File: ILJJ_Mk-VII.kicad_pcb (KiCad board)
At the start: 2 copper layers, 48.3 x 99.1 mm, 25 parts, among them J1 Conn_02x12, U1 74LS00, U10 74LS00, U11 74LS00, U2 74LS00, U3 74LS00, U4 74LS00, U5 74LS00, U6 74LS00, U7 74LS00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

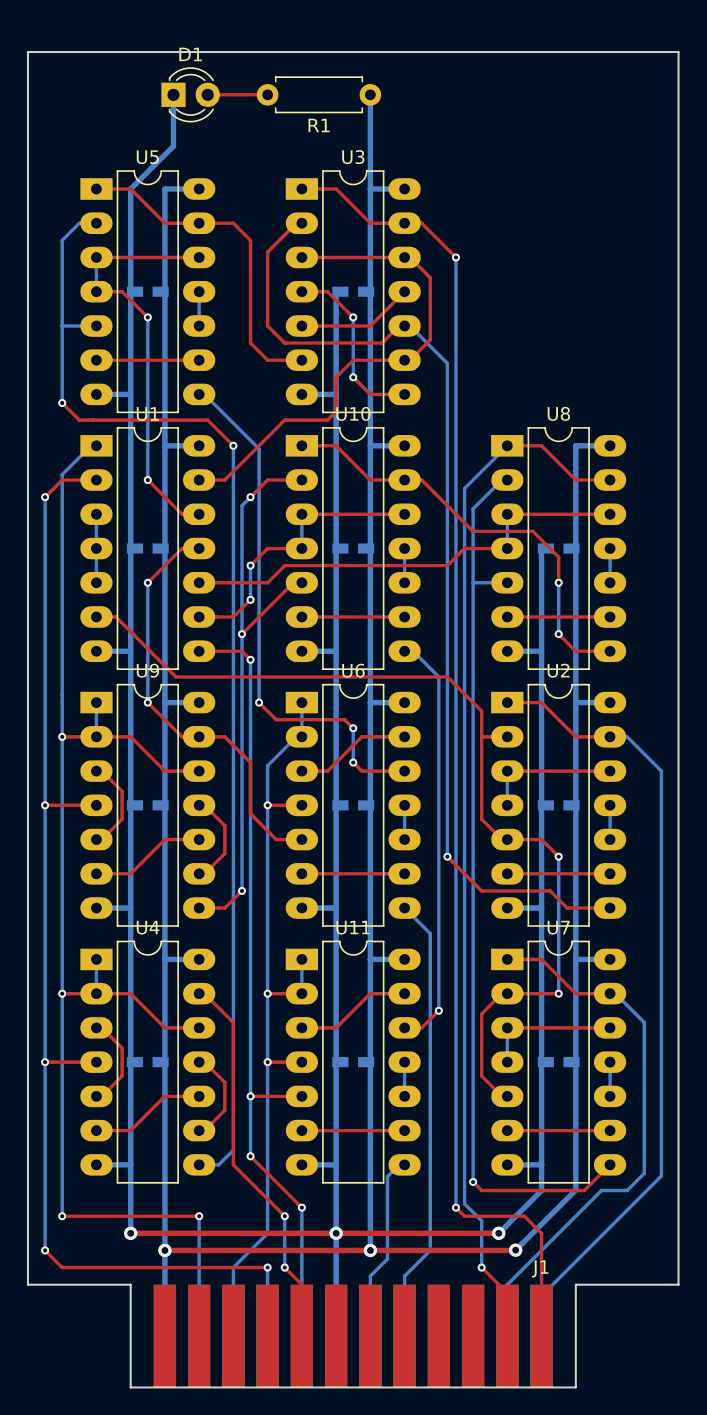
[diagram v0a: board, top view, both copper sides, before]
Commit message: [clean] 配線を微調整
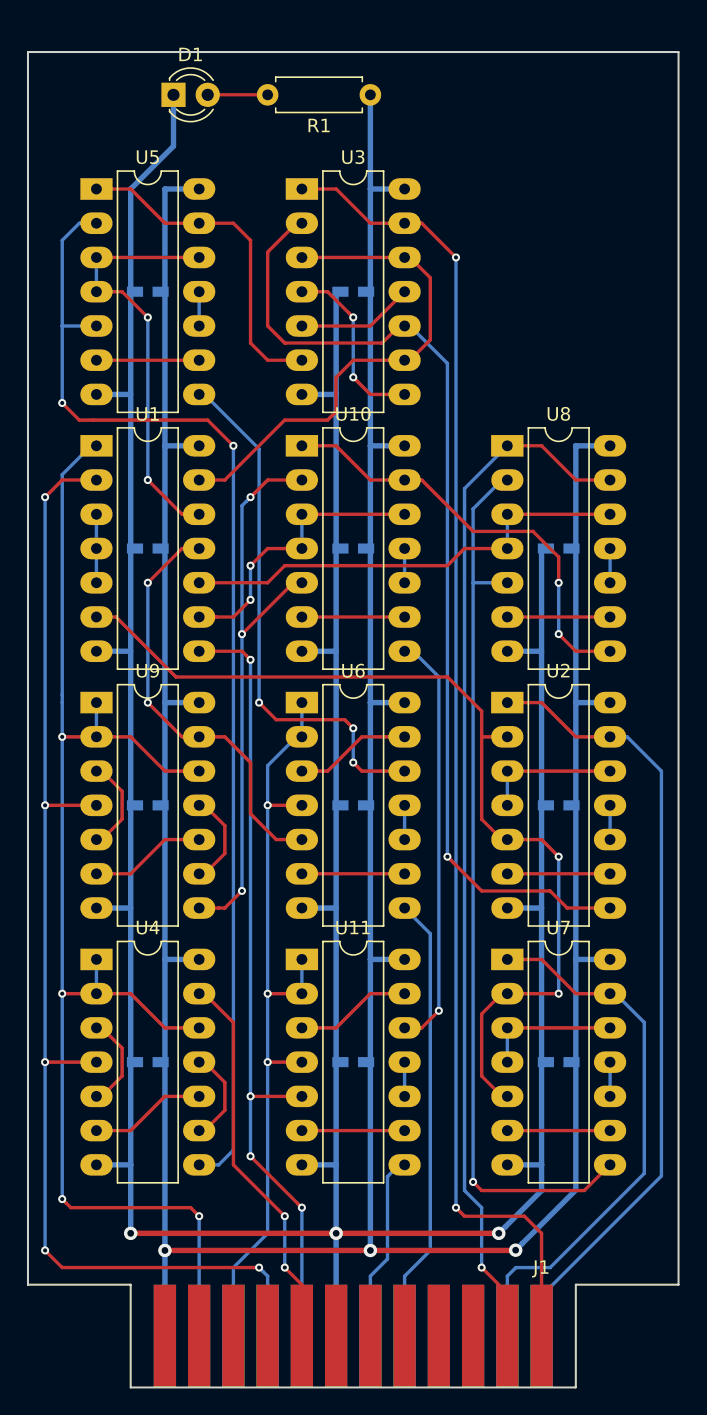
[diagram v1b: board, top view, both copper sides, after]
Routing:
- net /F2: track 105.0 -> 104.2 mm
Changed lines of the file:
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@@
     (thickness 1.6)
     (drawings 8)
-    (tracks 447)
+    (tracks 453)
     (zones 0)
     (modules 25)
@@
   (segment (start 111.76 104.14) (end 109.22 101.6) (width 0.25) (layer F.Cu) (net 4))
   (segment (start 106.68 101.6) (end 106.68 99.06) (width 0.25) (layer B.Cu) (net 4))
-  (via (at 114.3 137.16) (size 0.6) (drill 0.3) (layers F.Cu B.Cu) (net 4))
-  (segment (start 114.3 146.05) (end 114.3 137.16) (width 0.25) (layer B.Cu) (net 4))
-  (via (at 104.14 137.16) (size 0.6) (drill 0.3) (layers F.Cu B.Cu) (net 4))
-  (segment (start 114.3 137.16) (end 104.14 137.16) (width 0.25) (layer F.Cu) (net 4))
   (segment (start 106.28 80.01) (end 104.14 82.15) (width 0.25) (layer B.Cu) (net 4))
   (segment (start 104.14 98.494315) (end 104.14 99.06) (width 0.25) (layer B.Cu) (net 4))
@@
   (segment (start 104.14 101.6) (end 104.14 99.06) (width 0.25) (layer B.Cu) (net 4))
   (segment (start 106.68 101.6) (end 104.14 101.6) (width 0.25) (layer F.Cu) (net 4))
-  (segment (start 104.14 137.16) (end 104.14 101.6) (width 0.25) (layer B.Cu) (net 4))
   (via (at 104.14 120.65) (size 0.6) (drill 0.3) (layers F.Cu B.Cu) (net 4))
   (segment (start 106.68 120.65) (end 104.14 120.65) (width 0.25) (layer F.Cu) (net 4))
+  (via (at 114.3 137.16) (size 0.6) (drill 0.3) (layers F.Cu B.Cu) (net 4))
+  (segment (start 114.3 146.05) (end 114.3 137.16) (width 0.25) (layer B.Cu) (net 4))
+  (via (at 104.14 135.89) (size 0.6) (drill 0.3) (layers F.Cu B.Cu) (net 4))
+  (segment (start 104.14 101.6) (end 104.14 135.89) (width 0.25) (layer B.Cu) (net 4))
+  (segment (start 104.775 136.525) (end 104.439999 136.189999) (width 0.25) (layer F.Cu) (net 4))
+  (segment (start 104.439999 136.189999) (end 104.14 135.89) (width 0.25) (layer F.Cu) (net 4))
+  (segment (start 113.665 136.525) (end 104.775 136.525) (width 0.25) (layer F.Cu) (net 4))
+  (segment (start 114.3 137.16) (end 113.665 136.525) (width 0.25) (layer F.Cu) (net 4))
   (segment (start 116.84 146.05) (end 116.84 140.97) (width 0.25) (layer B.Cu) (net 5))
   (segment (start 116.84 140.97) (end 119.38 138.43) (width 0.25) (layer B.Cu) (net 5))
@@
   (segment (start 119.38 125.73) (end 119.38 120.65) (width 0.25) (layer B.Cu) (net 5))
   (segment (start 119.38 138.43) (end 119.38 125.73) (width 0.25) (layer B.Cu) (net 5))
-  (via (at 119.38 140.97) (size 0.6) (drill 0.3) (layers F.Cu B.Cu) (net 6))
-  (segment (start 119.38 146.05) (end 119.38 140.97) (width 0.25) (layer B.Cu) (net 6))
   (via (at 102.87 139.7) (size 0.6) (drill 0.3) (layers F.Cu B.Cu) (net 6))
-  (segment (start 104.14 140.97) (end 102.87 139.7) (width 0.25) (layer F.Cu) (net 6))
-  (segment (start 119.38 140.97) (end 104.14 140.97) (width 0.25) (layer F.Cu) (net 6))
   (via (at 102.87 83.82) (size 0.6) (drill 0.3) (layers F.Cu B.Cu) (net 6))
   (segment (start 104.14 82.55) (end 102.87 83.82) (width 0.25) (layer F.Cu) (net 6))
@@
   (segment (start 102.87 125.73) (end 102.87 106.68) (width 0.25) (layer B.Cu) (net 6))
   (segment (start 102.87 139.7) (end 102.87 125.73) (width 0.25) (layer B.Cu) (net 6))
+  (via (at 118.745 140.97) (size 0.6) (drill 0.3) (layers F.Cu B.Cu) (net 6))
+  (segment (start 119.38 141.605) (end 119.044999 141.269999) (width 0.25) (layer B.Cu) (net 6))
+  (segment (start 119.044999 141.269999) (end 118.745 140.97) (width 0.25) (layer B.Cu) (net 6))
+  (segment (start 102.87 139.7) (end 104.14 140.97) (width 0.25) (layer F.Cu) (net 6))
+  (segment (start 104.14 140.97) (end 118.320736 140.97) (width 0.25) (layer F.Cu) (net 6))
+  (segment (start 119.38 146.05) (end 119.38 141.605) (width 0.25) (layer B.Cu) (net 6))
+  (segment (start 118.320736 140.97) (end 118.745 140.97) (width 0.25) (layer F.Cu) (net 6))
   (segment (start 121.92 146.05) (end 121.92 143.0655) (width 0.25) (layer F.Cu) (net 7))
   (segment (start 121.92 142.24) (end 120.65 140.97) (width 0.25) (layer F.Cu) (net 7))
@@
   (segment (start 137.16 142.875) (end 135.255 140.97) (width 0.25) (layer F.Cu) (net 17))
   (segment (start 137.16 143.0655) (end 137.16 142.875) (width 0.25) (layer F.Cu) (net 17))
-  (segment (start 135.255 137.504998) (end 133.985 136.234998) (width 0.25) (layer B.Cu) (net 17))
-  (segment (start 135.255 140.97) (end 135.255 137.504998) (width 0.25) (layer B.Cu) (net 17))
-  (segment (start 133.985 136.234998) (end 133.985 83.185) (width 0.25) (layer B.Cu) (net 17))
   (segment (start 133.985 83.185) (end 137.16 80.01) (width 0.25) (layer B.Cu) (net 17))
+  (segment (start 133.985 135.255) (end 133.985 83.185) (width 0.25) (layer B.Cu) (net 17))
+  (segment (start 135.255 136.525) (end 133.985 135.255) (width 0.25) (layer B.Cu) (net 17))
+  (segment (start 135.255 140.97) (end 135.255 136.525) (width 0.25) (layer B.Cu) (net 17))
   (segment (start 139.7 118.11) (end 142.24 120.65) (width 0.25) (layer F.Cu) (net 18))
   (segment (start 142.24 120.65) (end 144.78 120.65) (width 0.25) (layer F.Cu) (net 18))
   (segment (start 137.16 118.11) (end 139.7 118.11) (width 0.25) (layer F.Cu) (net 18))
+  (segment (start 145.18 120.65) (end 144.78 120.65) (width 0.25) (layer B.Cu) (net 18))
   (segment (start 147.32 122.79) (end 145.18 120.65) (width 0.25) (layer B.Cu) (net 18))
-  (segment (start 146.05 135.255) (end 147.32 133.985) (width 0.25) (layer B.Cu) (net 18))
-  (segment (start 144.145 135.255) (end 146.05 135.255) (width 0.25) (layer B.Cu) (net 18))
-  (segment (start 137.16 146.05) (end 137.16 142.24) (width 0.25) (layer B.Cu) (net 18))
+  (segment (start 137.16 146.05) (end 137.16 141.605) (width 0.25) (layer B.Cu) (net 18))
   (segment (start 147.32 133.985) (end 147.32 122.79) (width 0.25) (layer B.Cu) (net 18))
-  (segment (start 145.18 120.65) (end 144.78 120.65) (width 0.25) (layer B.Cu) (net 18))
-  (segment (start 137.16 142.24) (end 144.145 135.255) (width 0.25) (layer B.Cu) (net 18))
+  (segment (start 137.795 140.97) (end 140.335 140.97) (width 0.25) (layer B.Cu) (net 18))
+  (segment (start 140.335 140.97) (end 147.32 133.985) (width 0.25) (layer B.Cu) (net 18))
+  (segment (start 137.16 141.605) (end 137.795 140.97) (width 0.25) (layer B.Cu) (net 18))
   (segment (start 121.92 60.96) (end 124.46 60.96) (width 0.25) (layer F.Cu) (net 19))
   (segment (start 124.46 60.96) (end 127 63.5) (width 0.25) (layer F.Cu) (net 19))

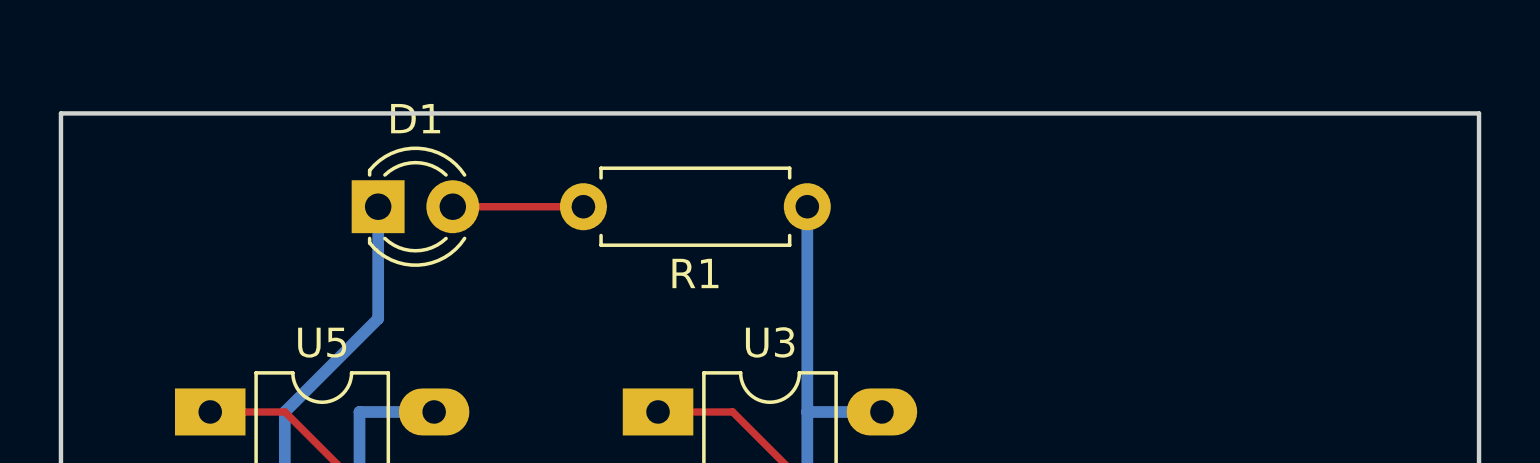
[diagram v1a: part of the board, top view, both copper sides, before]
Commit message: [add] ネジ穴
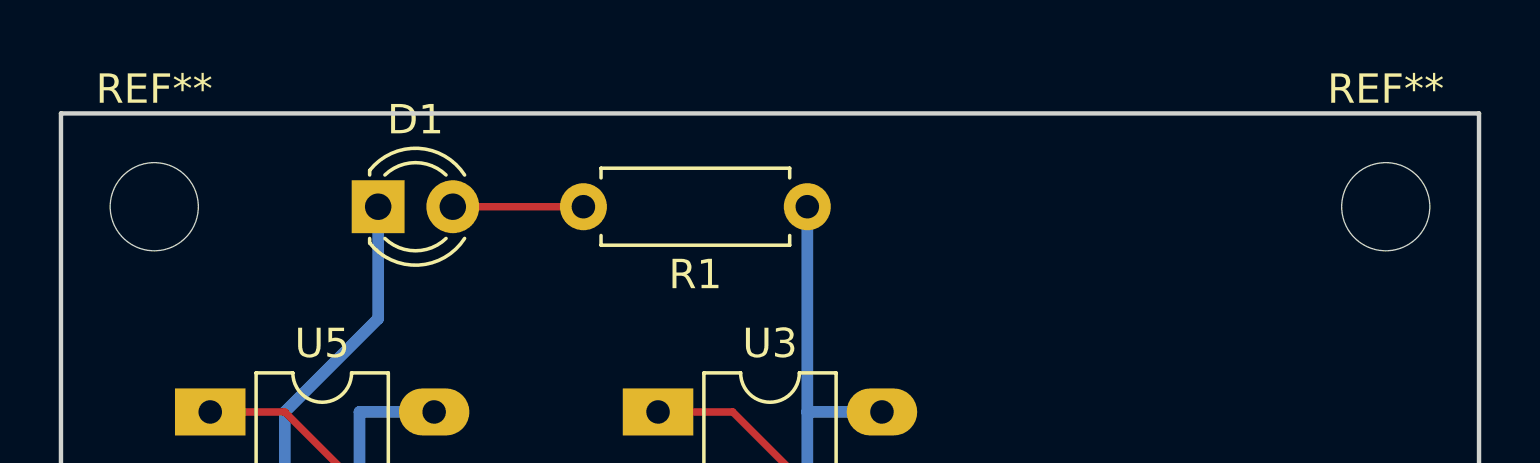
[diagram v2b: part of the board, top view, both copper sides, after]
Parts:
- added REF**: MountingHole_3mm, Mounting_Holes:MountingHole_3mm, F.Cu at (146.7, 54.0)
- added REF**: MountingHole_3mm, Mounting_Holes:MountingHole_3mm, F.Cu at (104.8, 54.0)
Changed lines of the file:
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@@
     (tracks 453)
     (zones 0)
-    (modules 25)
+    (modules 27)
     (nets 62)
   )
@@
     (add_net VCC)
   )
+  (module Mounting_Holes:MountingHole_3mm (layer F.Cu)
+    (at 146.685 53.975)
+    (descr "Mounting Hole 3mm, no annular")
+    (tags "mounting hole 3mm no annular")
+    (attr virtual)
+    (fp_text reference REF** (at 0 -4) (layer F.SilkS)
+      (effects (font (size 1 1) (thickness 0.15)))
+    )
+    (fp_text value MountingHole_3mm (at 0 4) (layer F.Fab)
+      (effects (font (size 1 1) (thickness 0.15)))
+    )
+    (fp_circle (center 0 0) (end 3.25 0) (layer F.CrtYd) (width 0.05))
+    (fp_circle (center 0 0) (end 3 0) (layer Cmts.User) (width 0.15))
+    (fp_text user %R (at 0.3 0) (layer F.Fab)
+      (effects (font (size 1 1) (thickness 0.15)))
+    )
+    (pad 1 np_thru_hole circle (at 0 0) (size 3 3) (drill 3) (layers *.Cu *.Mask))
+  )
   (module Capacitors_SMD:C_0603_HandSoldering (layer B.Cu)
     (at 110.49 68.58 180)
@@
     )
   )
+  (module Mounting_Holes:MountingHole_3mm (layer F.Cu)
+    (at 104.775 53.975)
+    (descr "Mounting Hole 3mm, no annular")
+    (tags "mounting hole 3mm no annular")
+    (attr virtual)
+    (fp_text reference REF** (at 0 -4) (layer F.SilkS)
+      (effects (font (size 1 1) (thickness 0.15)))
+    )
+    (fp_text value MountingHole_3mm (at 0 4) (layer F.Fab)
+      (effects (font (size 1 1) (thickness 0.15)))
+    )
+    (fp_text user %R (at 0.3 0) (layer F.Fab)
+      (effects (font (size 1 1) (thickness 0.15)))
+    )
+    (fp_circle (center 0 0) (end 3 0) (layer Cmts.User) (width 0.15))
+    (fp_circle (center 0 0) (end 3.25 0) (layer F.CrtYd) (width 0.05))
+    (pad 1 np_thru_hole circle (at 0 0) (size 3 3) (drill 3) (layers *.Cu *.Mask))
+  )
   (gr_line (start 101.6 142.24) (end 101.6 50.8) (layer Edge.Cuts) (width 0.15))
